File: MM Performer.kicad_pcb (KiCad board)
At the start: 4 copper layers, 74.8 x 84.8 mm, 41 parts, among them IC1 68000D, J1 VCC, J2 GND, U1 MC68030RC, U2 MC68881FN-SOC, U3 ATF16V8BJ, U4 ATF16V8BJ, U5 ATF16V8BJ, U6 ATF16V8BJ, U7 ATF16V8BJ

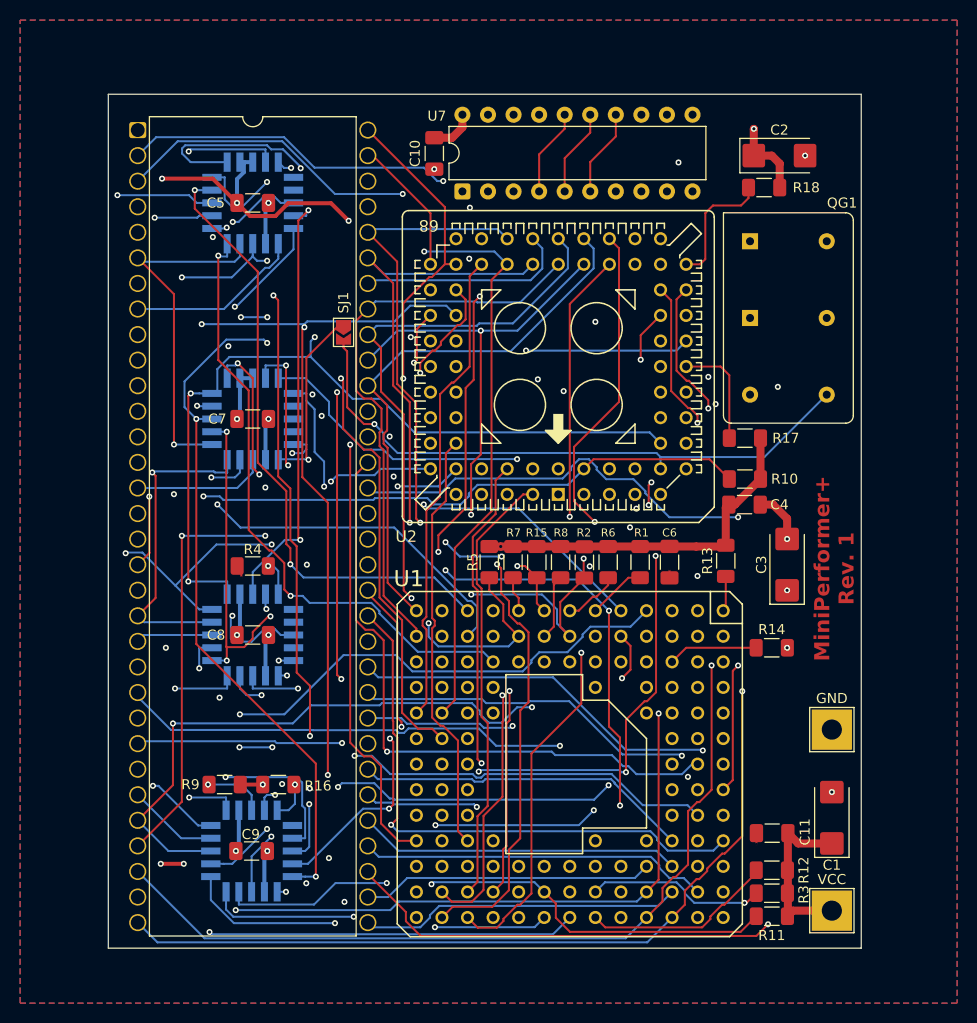
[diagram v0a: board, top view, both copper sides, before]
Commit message: Begin cleanup of the traces for the new revision
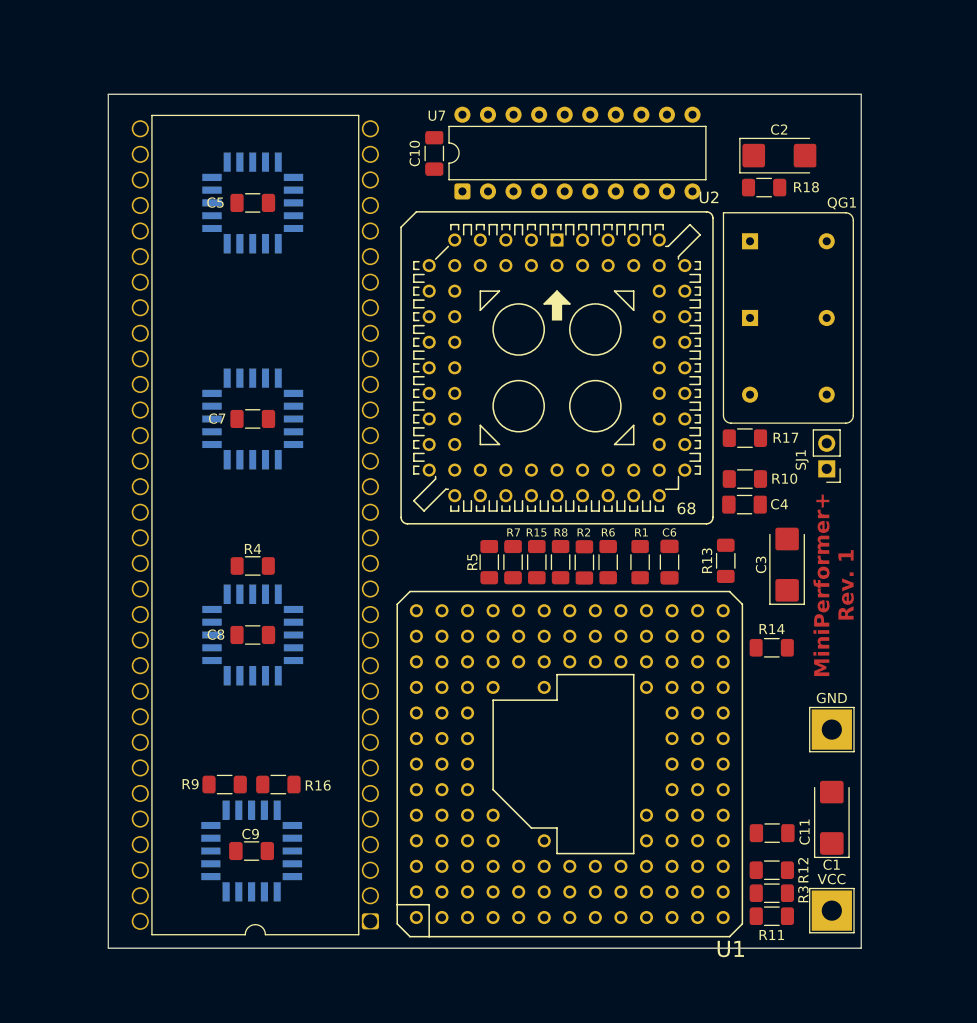
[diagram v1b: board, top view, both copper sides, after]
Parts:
- SJ1: footprint Jumper:SolderJumper-2_P1.3mm_Open_TrianglePad1.0x1.5mm -> Connector_PinHeader_2.54mm:PinHeader_1x02_P2.54mm_Vertical
- moved IC1 81.9 mm to (61.8, 134.5), turned to 180 degrees
- moved SJ1 49.9 mm to (107.2, 89.5), turned to 180 degrees
- moved U2 25.3 mm to (80.4, 66.8), turned to 0 degrees
- turned U1 to 90 degrees
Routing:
- net GND: track 659.5 -> 0.00 mm, vias 18 -> 0
- net VCC: track 655.3 -> 0.00 mm, vias 10 -> 0
- net //RESET_30: track 163.5 -> 0.00 mm, vias 6 -> 0
- net //R/W: track 157.1 -> 0.00 mm, vias 5 -> 0
- net /A22: track 135.2 -> 0.00 mm, vias 4 -> 0
- net /A21: track 128.4 -> 0.00 mm, vias 3 -> 0
- net /A1: track 128.4 -> 0.00 mm, vias 6 -> 0
- net /A4: track 124.4 -> 0.00 mm, vias 2 -> 0
- net /A2: track 121.4 -> 0.00 mm, vias 2 -> 0
- net //IPL2: track 120.0 -> 0.00 mm, vias 2 -> 0
- net //FPUCS: track 113.0 -> 0.00 mm, vias 5 -> 0
- net /A3: track 111.6 -> 0.00 mm, vias 5 -> 0
- net /C8M.PDS: track 105.5 -> 0.00 mm, vias 3 -> 0
- net /A0: track 105.2 -> 0.00 mm, vias 4 -> 0
- net //AS_30: track 105.2 -> 0.00 mm, vias 5 -> 0
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- removed copper zone on B.Cu, net GND
- removed copper zone on F.Cu, net GND
- removed copper zone on In1.Cu, net GND
- removed copper zone on In2.Cu, net GND

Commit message: Reorganize placement on the PCB
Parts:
- added C12: 100nF, Capacitor_SMD:C_1206_3216Metric_Pad1.33x1.80mm_HandSolder, B.Cu at (85.4, 106.9)
- added C13: 100nF, Capacitor_SMD:C_1206_3216Metric_Pad1.33x1.80mm_HandSolder, B.Cu at (85.3, 122.2)
- added C14: 100nF, Capacitor_SMD:C_1206_3216Metric_Pad1.33x1.80mm_HandSolder, B.Cu at (81.3, 71.1)
- C11, C4, C6, R10, R17, R18, R2, R5, R8: moved to B.Cu
- moved R3 74.2 mm to (50.5, 78.0), turned to 180 degrees
- moved U3 64.4 mm to (50.5, 63.1)
- moved R9 64.3 mm to (48.2, 56.6)
- moved R16 64.3 mm to (53.1, 56.6)
- moved R13 47.2 mm to (66.4, 134.5), turned to -90 degrees
- moved U6 42.9 mm to (50.5, 127.5)
- moved R11 41.3 mm to (85.6, 96.0), turned to 180 degrees
- moved R14 40.6 mm to (71.5, 134.5), turned to -90 degrees
- moved R12 39.5 mm to (80.6, 96.0)
- moved R5 38.1 mm to (86.7, 134.5), turned to -90 degrees
- moved R7 37.3 mm to (86.7, 134.5), turned to -90 degrees
- moved R1 36.9 mm to (79.1, 134.5), turned to -90 degrees
- moved R15 36.2 mm to (84.2, 134.5), turned to -90 degrees
- moved R6 35.9 mm to (81.7, 134.5), turned to -90 degrees
- moved R8 35.9 mm to (84.2, 134.5), turned to -90 degrees
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
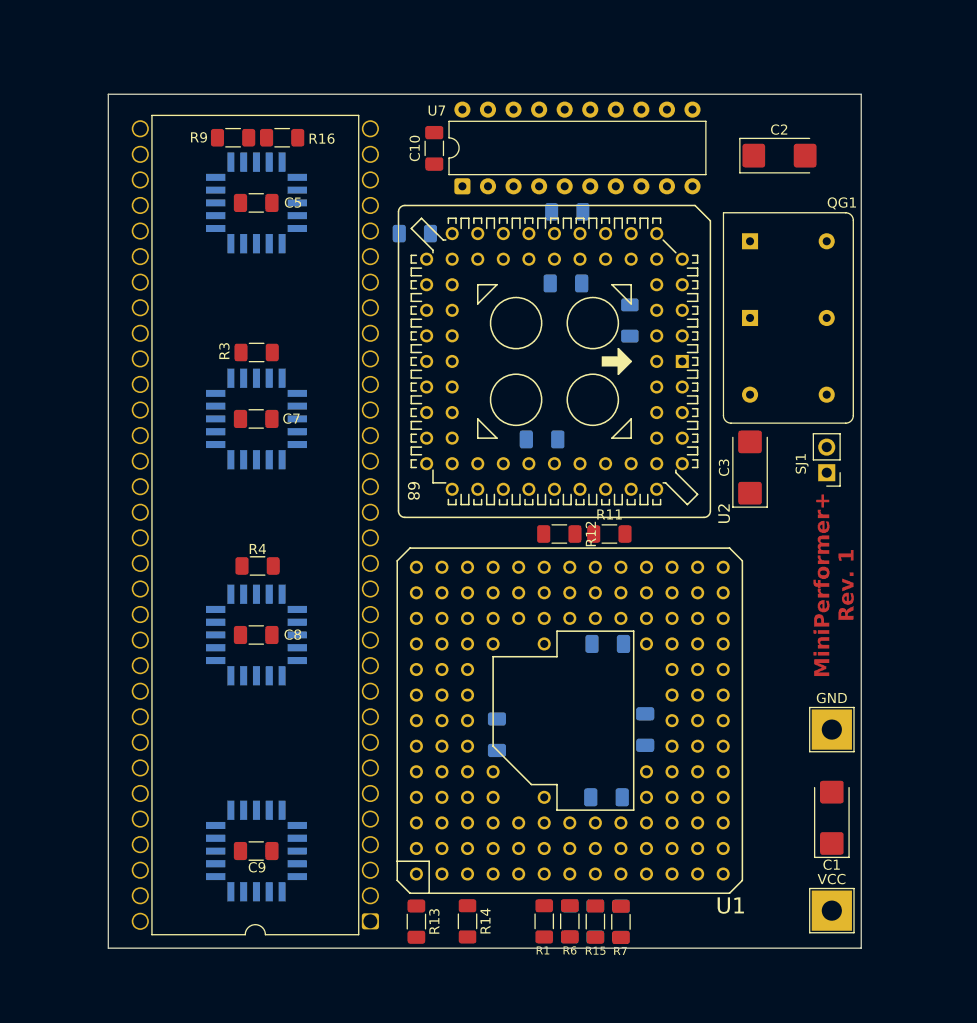
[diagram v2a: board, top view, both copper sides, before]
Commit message: Reorganize the board again
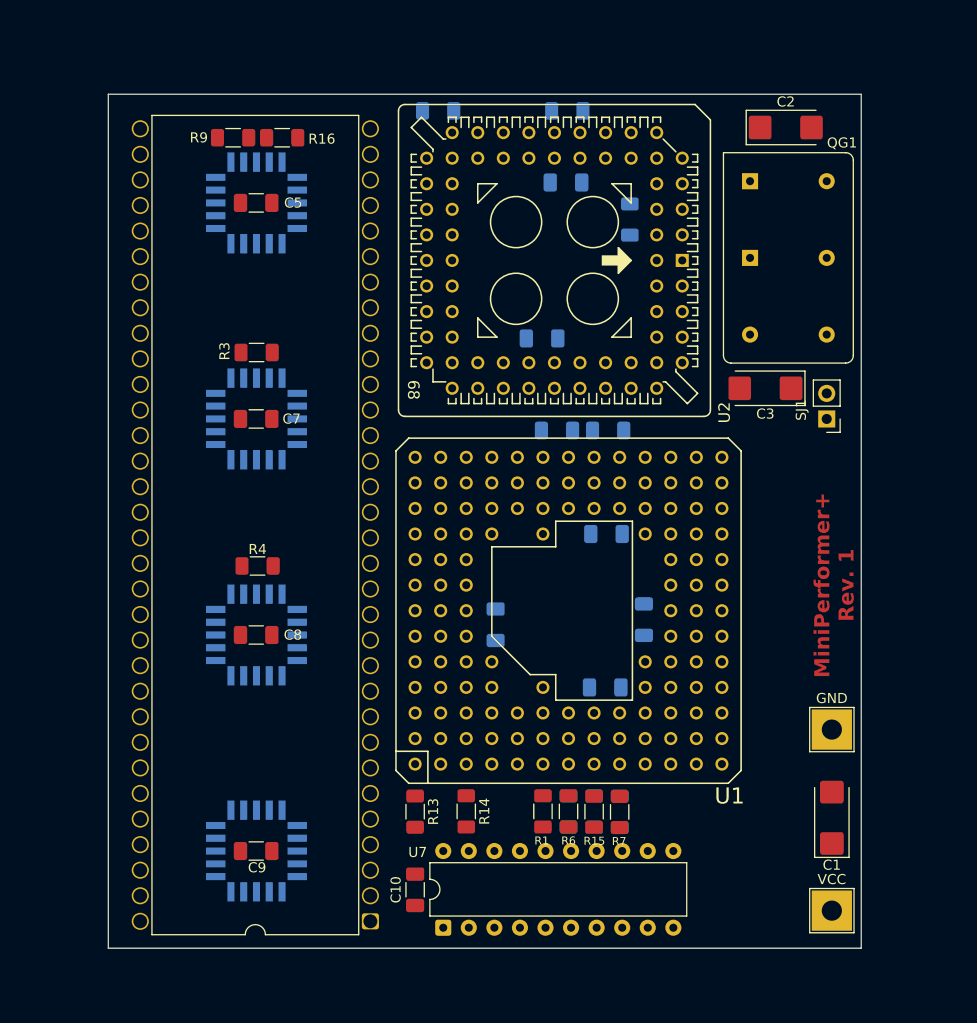
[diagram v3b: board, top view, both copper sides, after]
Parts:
- R11, R12: moved to B.Cu
- moved C10 73.7 mm to (66.3, 131.4)
- moved U7 73.7 mm to (69.1, 135.1)
- moved R18 12.4 mm to (68.6, 54.0)
- moved C13 10.9 mm to (85.2, 111.3)
- moved R13 10.9 mm to (66.3, 123.6)
- moved R15 10.9 mm to (84.1, 123.6)
- moved R8 10.9 mm to (84.1, 123.6)
- moved C11 10.9 mm to (89.0, 104.5)
- moved C12 10.9 mm to (85.3, 96.0)
- moved C6 10.9 mm to (74.3, 105.0)
- moved R1 10.9 mm to (79.0, 123.6)
- moved R14 10.9 mm to (71.4, 123.6)
- moved R2 10.9 mm to (81.5, 123.6)
- moved R6 10.9 mm to (81.5, 123.6)
- moved U1 10.9 mm to (81.5, 103.6)
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
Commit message: Initial routing of clock and power traces
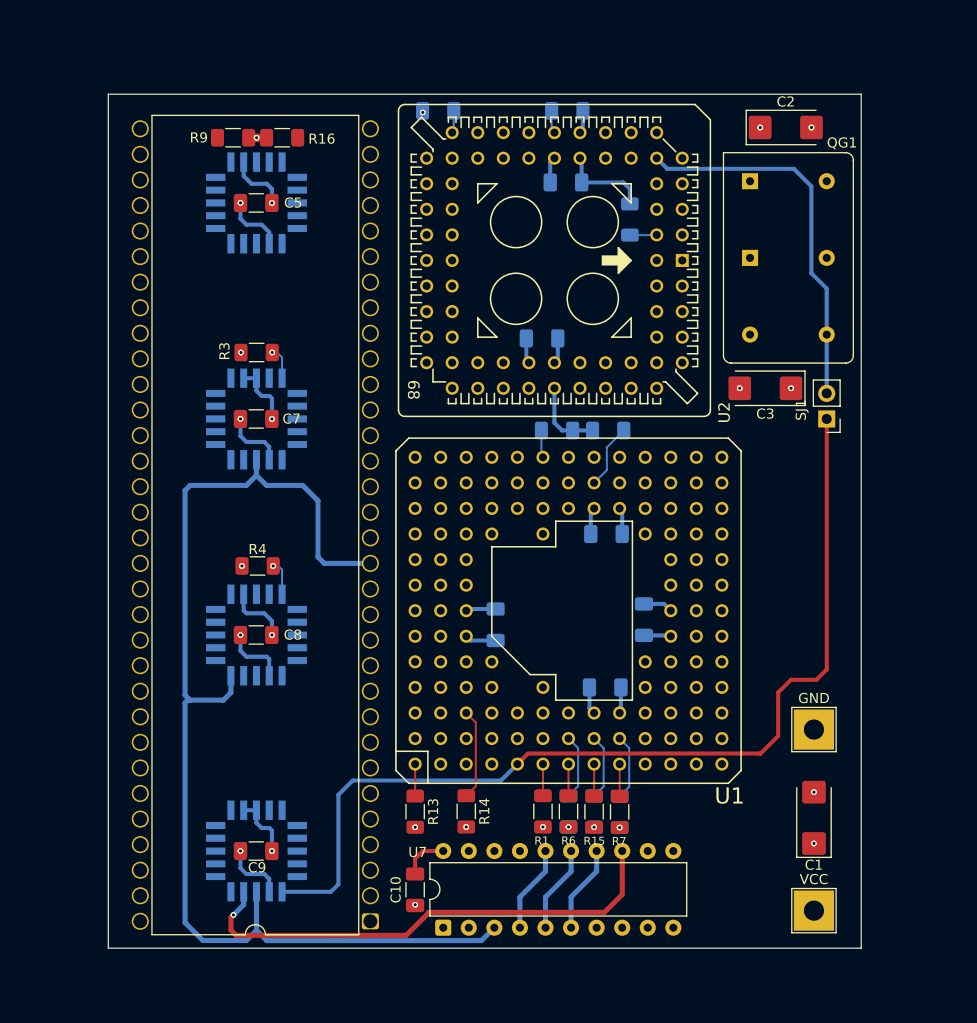
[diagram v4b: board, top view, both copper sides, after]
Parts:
- moved C1 1.78 mm to (105.9, 124.2)
- moved J1 1.78 mm to (105.9, 133.4)
- moved J2 1.78 mm to (105.9, 115.4)
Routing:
- net VCC: track 0.00 -> 815.6 mm, vias 0 -> 17
- net GND: track 0.00 -> 730.6 mm, vias 0 -> 8
- net /C8M.PDS: track 0.00 -> 113.7 mm
- net /CLK_30: track 0.00 -> 95.9 mm
- net /C16M: track 0.00 -> 49.4 mm, vias 0 -> 1
- net /FPUCLK: track 0.00 -> 37.7 mm
- net //BGACK_30: track 0.00 -> 9.02 mm
- net Net-(U7-I5): track 0.00 -> 8.67 mm
- net Net-(U7-I3): track 0.00 -> 8.67 mm
- net Net-(U7-I4): track 0.00 -> 8.67 mm
- net //AS_30: track 0.00 -> 6.53 mm
- net //HALT_30: track 0.00 -> 6.50 mm
- net //DSACK1: track 0.00 -> 6.48 mm
- net /CDIS: track 0.00 -> 6.43 mm
- net /P2.A17: track 0.00 -> 3.47 mm, vias 0 -> 1
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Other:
- board text removed: "MiniPerformer+ Rev. 1"

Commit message: Some rerouting of traces
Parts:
- removed SJ1: SJ, Connector_PinHeader_2.54mm:PinHeader_1x02_P2.54mm_Vertical
- added J3: FPU Clock, Connector_PinHeader_2.54mm:PinHeader_1x03_P2.54mm_Vertical, F.Cu at (101.3, 85.2)
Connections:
- QG1 pad 8: /FPUCLK -> Net-(J3-Pin_3)
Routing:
- net /SM_CLK16: track 0.00 -> 28.5 mm
- net Net-(J3-Pin_3): track 0.00 -> 9.33 mm
- net /CLK_30: track 95.9 -> 103.3 mm
- net /FPUCLK: track 37.7 -> 40.6 mm

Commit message: Update routing
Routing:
- net /CLK_30: track 103.3 -> 108.1 mm, vias 0 -> 1
- net VCC: track 815.6 -> 817.0 mm
- net /C16M: track 49.4 -> 48.6 mm, vias 1 -> 2
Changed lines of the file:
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@@
+	)
+	(segment
+		(start 48.945 127.508)
+		(end 49.784 127.508)
+		(width 0.4)
+		(layer "In1.Cu")
+		(net 1)
 	)
 	(segment
@@
 	)
 	(segment
+		(start 50.546 136.259)
+		(end 49.911 136.259)
+		(width 0.8)
+		(layer "In1.Cu")
+		(net 1)
+	)
+	(segment
 		(start 63.3 102.924)
 		(end 63.3 124.968)
@@
 	)
 	(segment
-		(start 48.945 127.508)
-		(end 48.945 136.182)
-		(width 0.4)
-		(layer "In1.Cu")
-		(net 1)
-	)
-	(segment
 		(start 89.154 111.252)
 		(end 90.424 109.982)
@@
 	(segment
 		(start 63.246 136.259)
+		(end 50.546 136.259)
+		(width 0.8)
+		(layer "In1.Cu")
+		(net 1)
+	)
+	(segment
+		(start 49.911 136.259)
 		(end 49.022 136.259)
 		(width 0.8)
@@
 	)
 	(segment
+		(start 50.546 128.27)
+		(end 50.546 136.259)
+		(width 0.4)
+		(layer "In1.Cu")
+		(net 1)
+	)
+	(segment
 		(start 48.996 77.978)
 		(end 48.996 78.206)
@@
 	)
 	(segment
+		(start 48.945 127.508)
+		(end 49.149 127.508)
+		(width 0.4)
+		(layer "In1.Cu")
+		(net 1)
+	)
+	(segment
+		(start 49.784 127.508)
+		(end 50.546 128.27)
+		(width 0.4)
+		(layer "In1.Cu")
+		(net 1)
+	)
+	(segment
 		(start 63.5 53.225)
 		(end 67.056 53.225)
@@
 	)
 	(segment
+		(start 66.294 134.112)
+		(end 66.407391 134.225391)
+		(width 0.4)
+		(layer "F.Cu")
+		(net 2)
+	)
+	(segment
 		(start 66.294 132.919)
 		(end 66.294 132.842)
@@
 		(start 105.918 121.656)
 		(end 105.918 121.666)
+		(width 0.4)
+		(layer "F.Cu")
+		(net 2)
+	)
+	(segment
+		(start 66.294 132.919)
+		(end 66.294 134.112)
 		(width 0.4)
 		(layer "F.Cu")
@@
 	)
 	(via
+		(at 66.407391 134.225391)
+		(size 0.6)
+		(drill 0.3)
+		(layers "F.Cu" "B.Cu")
+		(net 2)
+	)
+	(via
 		(at 98.542 81.534)
 		(size 0.6)
@@
 	)
 	(via
-		(at 66.294 132.842)
-		(size 0.6)
-		(drill 0.3)
-		(layers "F.Cu" "B.Cu")
-		(net 2)
-	)
-	(via
 		(at 52.07 106.045)
 		(size 0.6)
@@
 	)
 	(segment
+		(start 66.407391 134.225391)
+		(end 67.056 134.874)
+		(width 0.4)
+		(layer "In2.Cu")
+		(net 2)
+	)
+	(segment
 		(start 76.454 93.472)
 		(end 75.184 94.742)
@@
 	)
 	(segment
-		(start 66.777576 134.341576)
-		(end 66.294 133.858)
-		(width 0.4)
-		(layer "In2.Cu")
-		(net 2)
-	)
-	(segment
 		(start 63.3 76.708)
 		(end 63.3 62.738)
@@
 	)
 	(segment
-		(start 66.294 133.858)
-		(end 66.294 132.842)
-		(width 0.4)
-		(layer "In2.Cu")
-		(net 2)
-	)
-	(segment
 		(start 91.694 108.712)
 		(end 92.945 107.461)
@@
 	)
 	(segment
-		(start 67.564 134.341576)
-		(end 66.777576 134.341576)
-		(width 0.4)
-		(layer "In2.Cu")
-		(net 2)
-	)
-	(segment
 		(start 81.534 93.472)
 		(end 82.785 92.221)
@@
 	(segment
 		(start 65.786 136.144)
-		(end 67.564 134.366)
+		(end 67.056 134.874)
 		(width 0.8)
 		(layer "In2.Cu")
@@
 		(start 108.343 53.225)
 		(end 105.918 53.225)
+		(width 0.8)
+		(layer "In2.Cu")
+		(net 2)
+	)
+	(segment
+		(start 67.056 134.874)
+		(end 67.564 134.366)
 		(width 0.8)
 		(layer "In2.Cu")
@@
 	)
 	(segment
-		(start 107.569 124.968)
-		(end 108.712 123.825)
-		(width 0.4)
-		(layer "B.Cu")
+		(start 106.68 130.175)
+		(end 108.712 128.143)
+		(width 0.4)
+		(layer "F.Cu")
 		(net 82)
 	)
 	(segment
-		(start 101.346 87.249)
+		(start 101.981 87.63)
+		(end 101.346 86.995)
+		(width 0.4)
+		(layer "F.Cu")
+		(net 82)
+	)
+	(segment
+		(start 86.36 130.175)
+		(end 106.68 130.175)
+		(width 0.4)
+		(layer "F.Cu")
+		(net 82)
+	)
+	(segment
+		(start 108.712 89.535)
+		(end 106.807 87.63)
+		(width 0.4)
+		(layer "F.Cu")
+		(net 82)
+	)
+	(segment
+		(start 108.712 128.143)
+		(end 108.712 89.535)
+		(width 0.4)
+		(layer "F.Cu")
+		(net 82)
+	)
+	(segment
+		(start 85.217 131.318)
+		(end 86.36 130.175)
+		(width 0.4)
+		(layer "F.Cu")
+		(net 82)
+	)
+	(segment
+		(start 101.346 86.995)
 		(end 101.346 85.217)
 		(width 0.4)
-		(layer "B.Cu")
+		(layer "F.Cu")
 		(net 82)
 	)
 	(segment
-		(start 108.712 123.825)
-		(end 108.712 89.789)
-		(width 0.4)
-		(layer "B.Cu")
+		(start 68.707 131.318)
+		(end 85.217 131.318)
+		(width 0.4)
+		(layer "F.Cu")
 		(net 82)
 	)
 	(segment
-		(start 58.5355 130.683)
-		(end 62.484 130.683)
-		(width 0.4)
-		(layer "B.Cu")
+		(start 106.807 87.63)
+		(end 101.981 87.63)
+		(width 0.4)
+		(layer "F.Cu")
 		(net 82)
 	)
-	(segment
-		(start 101.727 87.63)
-		(end 101.346 87.249)
-		(width 0.4)
-		(layer "B.Cu")
+	(via
+		(at 68.707 131.318)
+		(size 0.6)
+		(drill 0.3)
+		(layers "F.Cu" "B.Cu")
 		(net 82)
 	)
 	(segment
-		(start 103.265 126.224)
-		(end 104.521 124.968)
+		(start 53.0715 131.5605)
+		(end 53.0715 132.3195)
 		(width 0.4)
 		(layer "B.Cu")
@@
 	)
 	(segment
-		(start 108.712 89.789)
-		(end 106.553 87.63)
+		(start 67.691 132.969)
+		(end 67.691 132.334)
 		(width 0.4)
 		(layer "B.Cu")
@@
 	)
 	(segment
-		(start 62.484 130.683)
-		(end 66.943 126.224)
+		(start 67.437 133.223)
+		(end 67.691 132.969)
 		(width 0.4)
 		(layer "B.Cu")
@@
 	)
 	(segment
-		(start 57.658 131.5605)
-		(end 58.5355 130.683)
+		(start 53.0715 132.3195)
+		(end 53.975 133.223)
 		(width 0.4)
 		(layer "B.Cu")
@@
 	)
 	(segment
-		(start 106.553 87.63)
-		(end 101.727 87.63)
+		(start 53.975 133.223)
+		(end 67.437 133.223)
 		(width 0.4)
 		(layer "B.Cu")
@@
 	)
 	(segment
-		(start 104.521 124.968)
-		(end 107.569 124.968)
-		(width 0.4)
-		(layer "B.Cu")
-		(net 82)
-	)
-	(segment
-		(start 66.943 126.224)
-		(end 103.265 126.224)
-		(width 0.4)
-		(layer "B.Cu")
-		(net 82)
-	)
-	(segment
-		(start 53.0715 131.5605)
-		(end 57.658 131.5605)
+		(start 67.691 132.334)
+		(end 68.707 131.318)
 		(width 0.4)
 		(layer "B.Cu")
@@
 	)
 	(segment
-		(start 67.669792 133.604)
-		(end 65.383792 135.89)
+		(start 85.968 133.604)
+		(end 86.868 132.704)
 		(width 0.5)
 		(layer "F.Cu")
@@
 	)
 	(segment
-		(start 85.09 133.604)
-		(end 67.669792 133.604)
+		(start 68.513708 133.604)
+		(end 85.968 133.604)
 		(width 0.5)
 		(layer "F.Cu")
@@
 	)
 	(segment
-		(start 86.868 131.826)
-		(end 85.09 133.604)
+		(start 67.837 135.001)
+		(end 67.837 134.280708)
 		(width 0.5)
 		(layer "F.Cu")
@@
 	)
 	(segment
-		(start 48.006 135.382)
-		(end 48.006 134.097)
+		(start 49.657 135.89)
+		(end 66.948 135.89)
 		(width 0.5)
 		(layer "F.Cu")
@@
 	)
 	(segment
-		(start 48.514 135.89)
-		(end 48.006 135.382)
-		(width 0.5)
+		(start 49.276 135.509)
+		(end 49.657 135.89)
+		(width 0.4)
 		(layer "F.Cu")
 		(net 123)
 	)
 	(segment
-		(start 48.006 134.097)
-		(end 48.245 133.858)
-		(width 0.5)
+		(start 49.276 133.223)
+		(end 49.276 135.509)
+		(width 0.4)
 		(layer "F.Cu")
 		(net 123)
 	)
 	(segment
-		(start 65.383792 135.89)
-		(end 48.514 135.89)
+		(start 66.948 135.89)
+		(end 67.837 135.001)
 		(width 0.5)
 		(layer "F.Cu")
@@
 	)
 	(segment
-		(start 86.868 127.508)
-		(end 86.868 131.826)
+		(start 67.837 134.280708)
+		(end 68.513708 133.604)
 		(width 0.5)
 		(layer "F.Cu")
@@
 	)
 	(via
-		(at 48.245 133.858)
+		(at 86.868 132.704)
 		(size 0.6)
 		(drill 0.3)
@@
 		(net 123)
 	)
-	(segment
-		(start 49.2615 132.8415)
-		(end 49.2615 131.5605)
-		(width 0.5)
-		(layer "B.Cu")
+	(via
+		(at 49.276 133.223)
+		(size 0.6)
+		(drill 0.3)
+		(layers "F.Cu" "B.Cu")
 		(net 123)
 	)
 	(segment
-		(start 48.245 133.858)
-		(end 49.2615 132.8415)
+		(start 86.868 132.704)
+		(end 86.868 127.508)
 		(width 0.5)
 		(layer "B.Cu")
 		(net 123)
+	)
+	(segment
+		(start 49.2615 133.2085)
+		(end 49.276 133.223)
+		(width 0.4)
+		(layer "B.Cu")
+		(net 123)
+	)
+	(segment
+		(start 49.2615 131.5605)
+		(end 49.2615 133.2085)
+		(width 0.4)
+		(layer "B.Cu")
+		(net 123)

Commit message: Move cap near CPU
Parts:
- moved C3 18.5 mm to (100.8, 100.1), turned to -90 degrees
- moved J3 4.26 mm to (102.1, 81.0)
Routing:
- net Net-(J3-Pin_3): track 9.33 -> 4.83 mm
- net /CLK_30: track 108.1 -> 111.8 mm
- net GND: track 730.4 -> 727.0 mm
- net /FPUCLK: track 40.6 -> 39.5 mm
- net VCC: track 817.0 -> 817.8 mm
